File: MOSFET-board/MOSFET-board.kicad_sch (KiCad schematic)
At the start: 5 parts, among them J1 PCIE-LP-01-01-F-DV-A-TR, J2 DB15_Female, J3 DB15_Female, U11 PCF8575_Breakout

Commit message: Progress on revising ground boards.
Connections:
- net +12V: no longer J2.10 (P10), J2.11 (P111), J2.12 (P12), J2.13 (P13), J2.9 (P9), J3.10 (P10), J3.11 (P111), J3.12 (P12), J3.13 (P13), J3.9 (P9)
- new net -7 V: J2.10 (P10), J2.11 (P111), J2.12 (P12), J2.13 (P13), J2.9 (P9), J3.10 (P10), J3.11 (P111), J3.12 (P12), J3.13 (P13), J3.9 (P9)

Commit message: Further revision. Two batteries system.
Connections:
- net -7 V renamed -7V
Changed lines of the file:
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@@
+    (stroke (width 0) (type default))
+  )
+  (wire (pts (xy 175.006 113.03) (xy 175.006 114.808))
     (stroke (width 0) (type default))
   )
@@
     )
   )
+  (global_label "BAT2_+" (shape input) (at 169.418 114.808 270) (fields_autoplaced)
+    (effects (font (size 1.27 1.27)) (justify right))
+    (property "Intersheetrefs" "${INTERSHEET_REFS}" (at 169.418 124.8689 90)
+      (effects (font (size 1.27 1.27)) (justify right) hide)
+    )
+  )
   (global_label "I2C_SDA" (shape input) (at 46.99 120.65 270) (fields_autoplaced)
     (effects (font (size 1.27 1.27)) (justify right))
@@
     )
   )
+  (global_label "-7V" (shape input) (at 175.006 113.03 0) (fields_autoplaced)
+    (effects (font (size 1.27 1.27)) (justify left))
+    (property "Intersheetrefs" "${INTERSHEET_REFS}" (at 181.8617 113.03 0)
+      (effects (font (size 1.27 1.27)) (justify left) hide)
+    )
+  )
   (global_label "PYRO9" (shape input) (at 165.608 78.232 180) (fields_autoplaced)
     (effects (font (size 1.27 1.27)) (justify right))
@@
     )
   )
-  (global_label "-7 V" (shape input) (at 26.416 167.132 270) (fields_autoplaced)
-    (effects (font (size 1.27 1.27)) (justify right))
-    (property "Intersheetrefs" "${INTERSHEET_REFS}" (at 26.416 174.9553 90)
+  (global_label "BAT2_-" (shape input) (at 26.416 167.132 270) (fields_autoplaced)
+    (effects (font (size 1.27 1.27)) (justify right))
+    (property "Intersheetrefs" "${INTERSHEET_REFS}" (at 26.416 177.1929 90)
       (effects (font (size 1.27 1.27)) (justify right) hide)
     )
@@
     )
   )
-  (global_label "-7 V" (shape input) (at 68.326 166.878 270) (fields_autoplaced)
-    (effects (font (size 1.27 1.27)) (justify right))
-    (property "Intersheetrefs" "${INTERSHEET_REFS}" (at 68.326 174.7013 90)
+  (global_label "BAT2_-" (shape input) (at 68.326 166.878 270) (fields_autoplaced)
+    (effects (font (size 1.27 1.27)) (justify right))
+    (property "Intersheetrefs" "${INTERSHEET_REFS}" (at 68.326 176.9389 90)
+      (effects (font (size 1.27 1.27)) (justify right) hide)
+    )
+  )
+  (global_label "BAT2_-" (shape input) (at 175.006 114.808 270) (fields_autoplaced)
+    (effects (font (size 1.27 1.27)) (justify right))
+    (property "Intersheetrefs" "${INTERSHEET_REFS}" (at 175.006 124.8689 90)
       (effects (font (size 1.27 1.27)) (justify right) hide)
     )
@@
         )
       )
+    )
+  )
+  (symbol (lib_id "power:+5V") (at 169.418 114.808 0) (unit 1)
+    (in_bom yes) (on_board yes) (dnp no)
+    (property "Reference" "#PWR010" (at 169.418 118.618 0)
+      (effects (font (size 1.27 1.27)) hide)
+    )
+    (property "Value" "+5V" (at 168.91 110.49 0)
+      (effects (font (size 1.27 1.27)))
+    )
+    (property "Footprint" "" (at 169.418 114.808 0)
+      (effects (font (size 1.27 1.27)) hide)
+    )
+    (property "Datasheet" "" (at 169.418 114.808 0)
+      (effects (font (size 1.27 1.27)) hide)
+    )
+    (pin "1")
+    (instances
+      (project "MOSFET-board"
+        (path "/eeff6235-4c56-4b47-a90f-883101560994"
+          (reference "#PWR010") (unit 1)
+        )
+      )

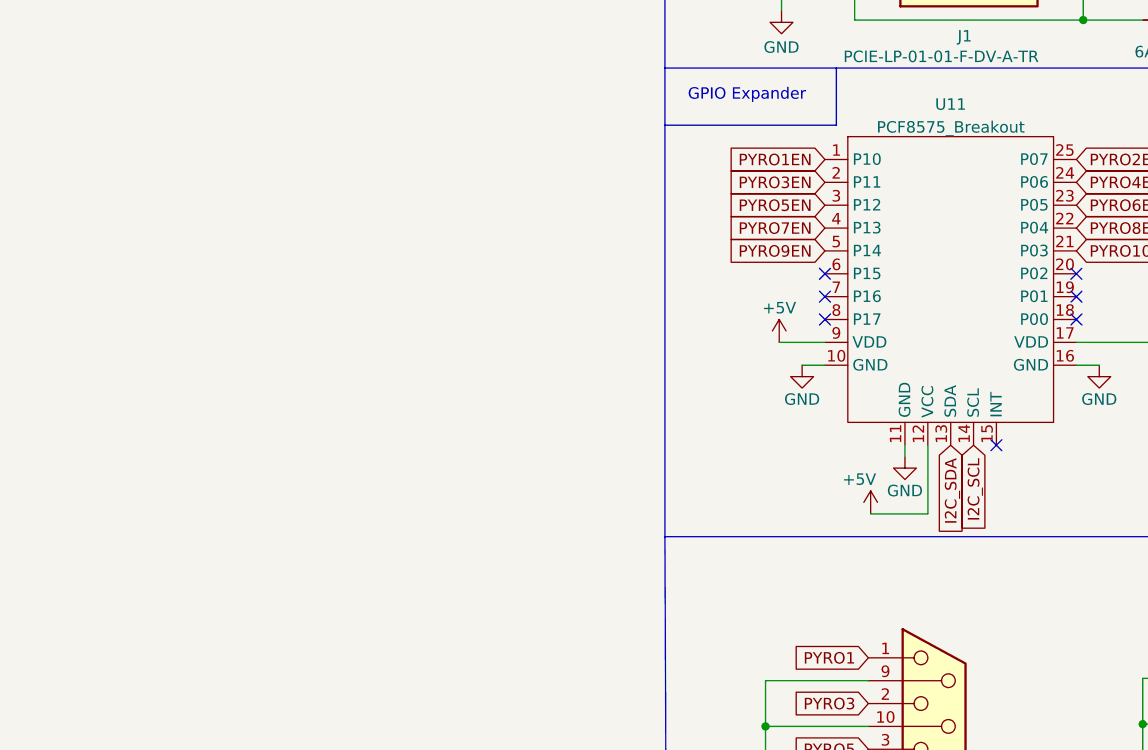
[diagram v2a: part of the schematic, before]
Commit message: Added level shifter for gpio expander.
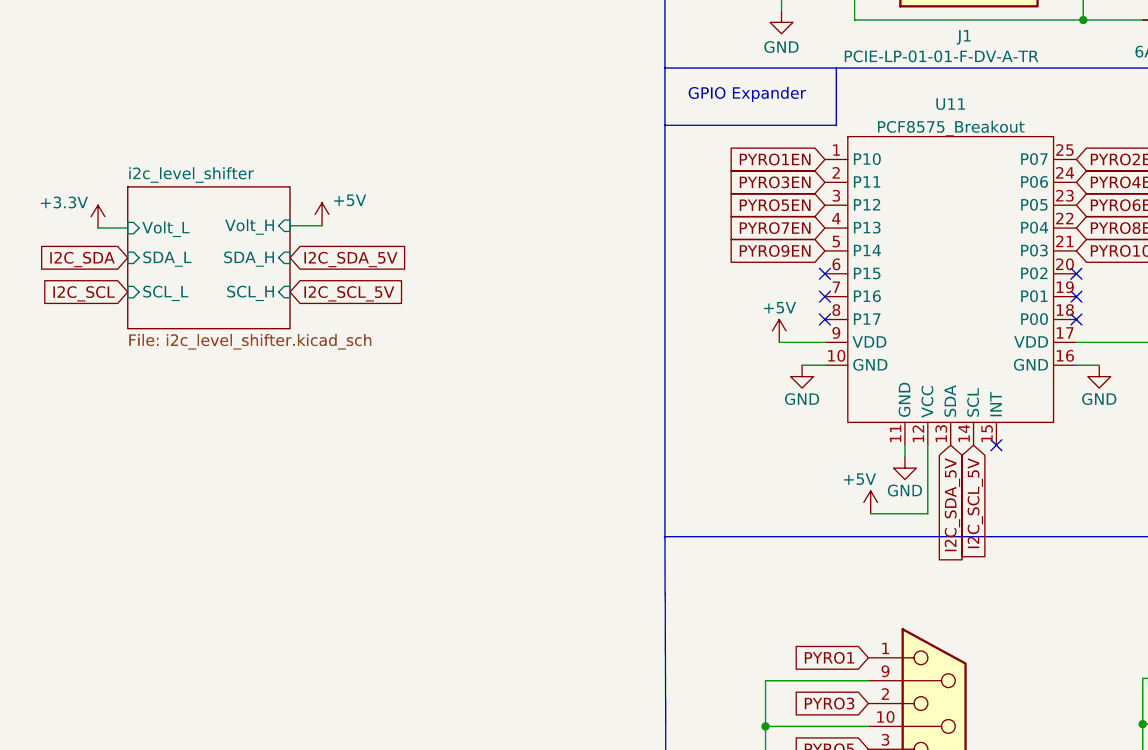
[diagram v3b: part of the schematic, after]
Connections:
- net I2C_SCL: no longer U11.14 (SCL)
- net I2C_SDA: no longer U11.13 (SDA)
- new net I2C_SCL_5V: U11.14 (SCL)
- new net I2C_SDA_5V: U11.13 (SDA)
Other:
- added sheet i2c_level_shifter (i2c_level_shifter.kicad_sch)
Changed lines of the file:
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@@
+    (stroke (width 0) (type default))
+  )
+  (wire (pts (xy -26.416 96.266) (xy -22.86 96.266))
     (stroke (width 0) (type default))
   )
@@
   )
   (wire (pts (xy 68.326 151.638) (xy 68.326 156.718))
+    (stroke (width 0) (type default))
+  )
+  (wire (pts (xy -47.752 96.52) (xy -44.45 96.52))
     (stroke (width 0) (type default))
   )
@@
     )
   )
-  (global_label "I2C_SDA" (shape input) (at 46.99 120.65 270) (fields_autoplaced)
-    (effects (font (size 1.27 1.27)) (justify right))
-    (property "Intersheetrefs" "${INTERSHEET_REFS}" (at 46.9106 130.6831 90)
+  (global_label "I2C_SDA" (shape input) (at -44.45 99.822 180) (fields_autoplaced)
+    (effects (font (size 1.27 1.27)) (justify right))
+    (property "Intersheetrefs" "${INTERSHEET_REFS}" (at -55.0552 99.822 0)
       (effects (font (size 1.27 1.27)) (justify right) hide)
     )
@@
     )
   )
-  (global_label "I2C_SCL" (shape input) (at 49.53 120.65 270) (fields_autoplaced)
-    (effects (font (size 1.27 1.27)) (justify right))
-    (property "Intersheetrefs" "${INTERSHEET_REFS}" (at 49.4506 130.6226 90)
+  (global_label "I2C_SCL" (shape input) (at -44.45 103.632 180) (fields_autoplaced)
+    (effects (font (size 1.27 1.27)) (justify right))
+    (property "Intersheetrefs" "${INTERSHEET_REFS}" (at -54.9947 103.632 0)
       (effects (font (size 1.27 1.27)) (justify right) hide)
     )
@@
     (property "Intersheetrefs" "${INTERSHEET_REFS}" (at 90.0913 104.3146 0)
       (effects (font (size 1.27 1.27)) (justify right) hide)
+    )
+  )
+  (global_label "I2C_SDA_5V" (shape input) (at -26.416 99.822 0) (fields_autoplaced)
+    (effects (font (size 1.27 1.27)) (justify left))
+    (property "Intersheetrefs" "${INTERSHEET_REFS}" (at -12.5451 99.822 0)
+      (effects (font (size 1.27 1.27)) (justify left) hide)
     )
   )
@@
     )
   )
+  (global_label "I2C_SCL_5V" (shape input) (at -26.416 103.632 0) (fields_autoplaced)
+    (effects (font (size 1.27 1.27)) (justify left))
+    (property "Intersheetrefs" "${INTERSHEET_REFS}" (at -12.6056 103.632 0)
+      (effects (font (size 1.27 1.27)) (justify left) hide)
+    )
+  )
   (global_label "PYRO9EN" (shape input) (at 33.02 99.06 180) (fields_autoplaced)
     (effects (font (size 1.27 1.27)) (justify right))
@@
     (effects (font (size 1.27 1.27)) (justify right))
     (property "Intersheetrefs" "${INTERSHEET_REFS}" (at 90.7928 81.9626 0)
+      (effects (font (size 1.27 1.27)) (justify right) hide)
+    )
+  )
+  (global_label "I2C_SCL_5V" (shape input) (at 49.53 120.65 270) (fields_autoplaced)
+    (effects (font (size 1.27 1.27)) (justify right))
+    (property "Intersheetrefs" "${INTERSHEET_REFS}" (at 49.53 134.4604 90)
       (effects (font (size 1.27 1.27)) (justify right) hide)
     )
@@
     (effects (font (size 1.27 1.27)) (justify right))
     (property "Intersheetrefs" "${INTERSHEET_REFS}" (at 21.4661 96.52 0)
+      (effects (font (size 1.27 1.27)) (justify right) hide)
+    )
+  )
+  (global_label "I2C_SDA_5V" (shape input) (at 46.99 120.65 270) (fields_autoplaced)
+    (effects (font (size 1.27 1.27)) (justify right))
+    (property "Intersheetrefs" "${INTERSHEET_REFS}" (at 46.99 134.5209 90)
       (effects (font (size 1.27 1.27)) (justify right) hide)
     )
@@
     )
   )
+  (symbol (lib_id "power:+3.3V") (at -47.752 96.52 0) (unit 1)
+    (in_bom yes) (on_board yes) (dnp no)
+    (property "Reference" "#PWR015" (at -47.752 100.33 0)
+      (effects (font (size 1.27 1.27)) hide)
+    )
+    (property "Value" "+3.3V" (at -51.562 93.726 0)
+      (effects (font (size 1.27 1.27)))
+    )
+    (property "Footprint" "" (at -47.752 96.52 0)
+      (effects (font (size 1.27 1.27)) hide)
+    )
+    (property "Datasheet" "" (at -47.752 96.52 0)
+      (effects (font (size 1.27 1.27)) hide)
+    )
+    (pin "1")
+    (instances
+      (project "MOSFET-board"
+        (path "/eeff6235-4c56-4b47-a90f-883101560994"
+          (reference "#PWR015") (unit 1)
+        )
+      )
+    )
+  )
   (symbol (lib_id "power:+3.3V") (at 163.83 139.446 0) (unit 1)
     (in_bom yes) (on_board yes) (dnp no)
@@
         (path "/eeff6235-4c56-4b47-a90f-883101560994"
           (reference "#PWR02") (unit 1)
+        )
+      )
+    )
+  )
+  (symbol (lib_id "power:+5V") (at -22.86 96.266 0) (unit 1)
+    (in_bom yes) (on_board yes) (dnp no)
+    (property "Reference" "#PWR016" (at -22.86 100.076 0)
+      (effects (font (size 1.27 1.27)) hide)
+    )
+    (property "Value" "+5V" (at -19.812 93.472 0)
+      (effects (font (size 1.27 1.27)))
+    )
+    (property "Footprint" "" (at -22.86 96.266 0)
+      (effects (font (size 1.27 1.27)) hide)
+    )
+    (property "Datasheet" "" (at -22.86 96.266 0)
+      (effects (font (size 1.27 1.27)) hide)
+    )
+    (pin "1")
+    (instances
+      (project "MOSFET-board"
+        (path "/eeff6235-4c56-4b47-a90f-883101560994"
+          (reference "#PWR016") (unit 1)
         )
       )
@@
       )
     )
+  )
+  (sheet (at -44.45 91.948) (size 18.034 15.748) (fields_autoplaced)
+    (stroke (width 0.1524) (type solid))
+    (fill (color 0 0 0 0.0000))
+    (property "Sheetname" "i2c_level_shifter" (at -44.45 91.2364 0)
+      (effects (font (size 1.27 1.27)) (justify left bottom))
+    )
+    (property "Sheetfile" "i2c_level_shifter.kicad_sch" (at -44.45 108.2806 0)
+      (effects (font (size 1.27 1.27)) (justify left top))
+    )
+    (pin "Volt_H" input (at -26.416 96.266 0)
+      (effects (font (size 1.27 1.27)) (justify right))
+    )
+    (pin "SDA_H" input (at -26.416 99.822 0)
+      (effects (font (size 1.27 1.27)) (justify right))
+    )
+    (pin "Volt_L" input (at -44.45 96.52 180)
+      (effects (font (size 1.27 1.27)) (justify left))
+    )
+    (pin "SCL_H" input (at -26.416 103.632 0)
+      (effects (font (size 1.27 1.27)) (justify right))
+    )
+    (pin "SCL_L" input (at -44.45 103.632 180)
+      (effects (font (size 1.27 1.27)) (justify left))
+    )
+    (pin "SDA_L" input (at -44.45 99.822 180)
+      (effects (font (size 1.27 1.27)) (justify left))
+    )
+    (instances
+      (project "MOSFET-board"
+        (path "/eeff6235-4c56-4b47-a90f-883101560994" (page "12"))
+      )
+    )

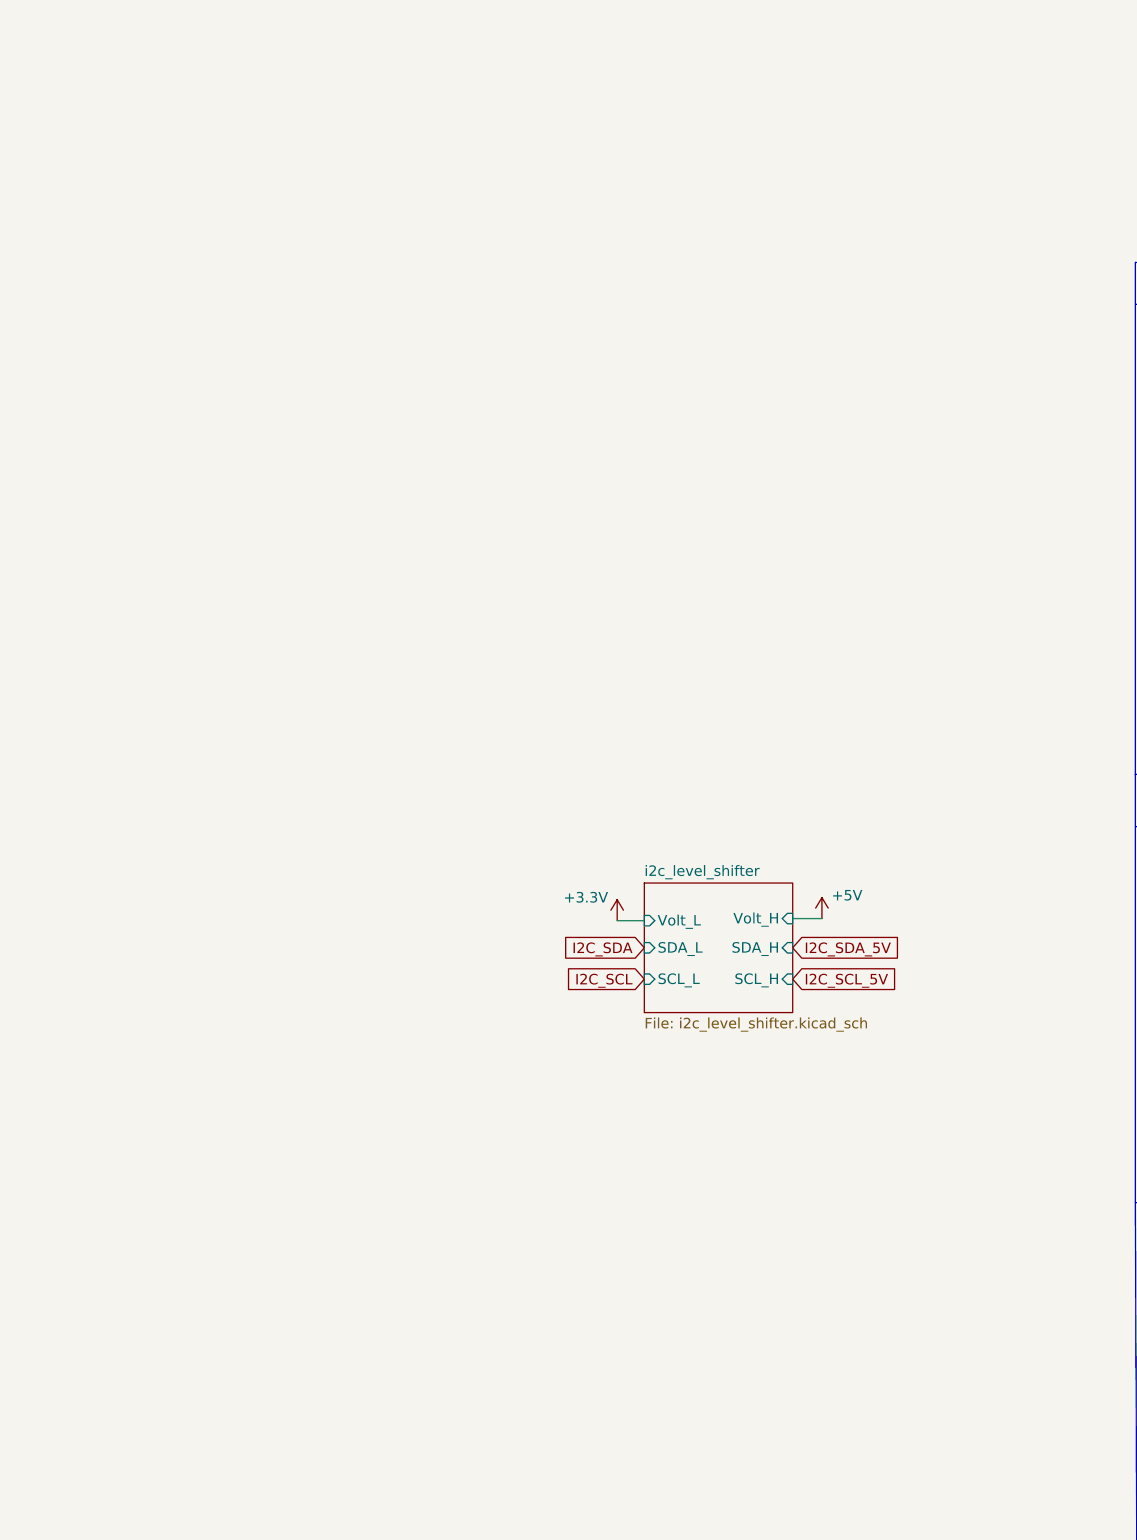
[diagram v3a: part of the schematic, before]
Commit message: Revising PCIe.
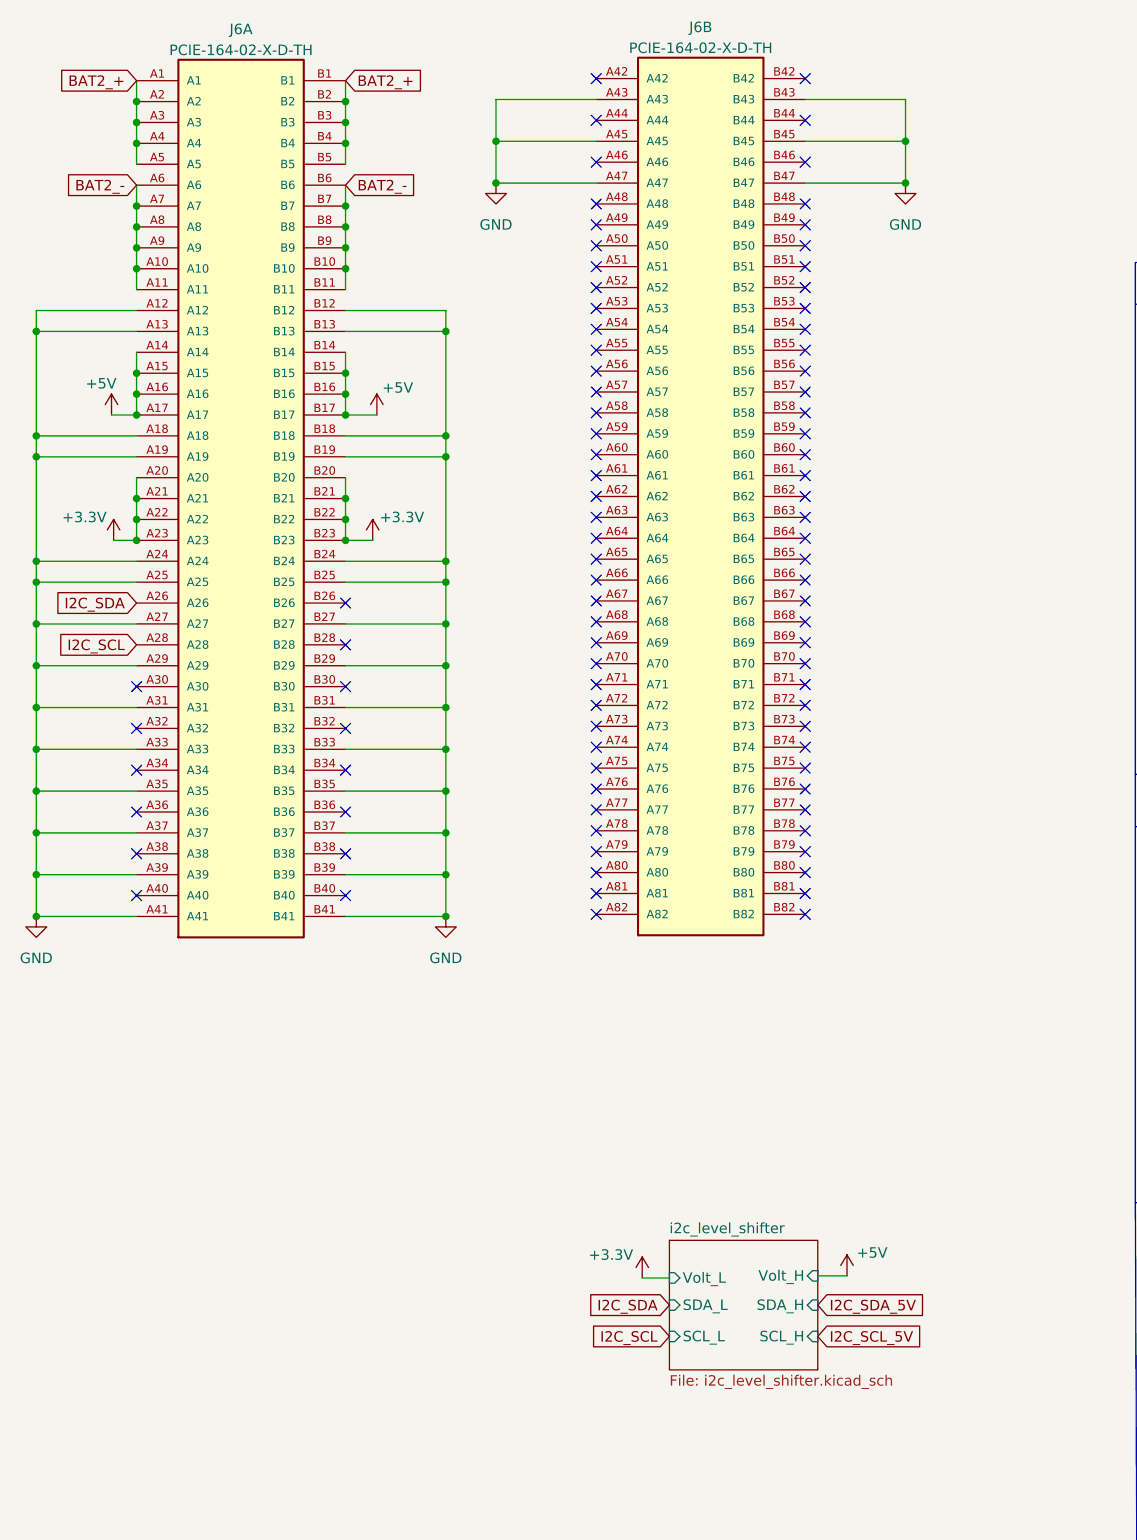
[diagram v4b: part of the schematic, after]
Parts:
- added J6: PCIE-164-02-X-D-TH, PCIE-164-02-X-D-TH:SAMTEC_PCIE-164-02-X-D-TH, symbol PCIE-164-02-X-D-TH:PCIE-164-02-X-D-TH
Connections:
- net +3.3V: now also J6.A20, J6.A21, J6.A22, J6.A23, J6.B20, J6.B21, J6.B22, J6.B23
- net +5V: now also J6.A1, J6.A14, J6.A15, J6.A16, J6.A17, J6.A2, J6.A3, J6.A4, J6.A5, J6.B1, J6.B14, J6.B15, J6.B16, J6.B17, J6.B2, J6.B3, J6.B4, J6.B5
- net -7V: now also J6.A10, J6.A11, J6.A6, J6.A7, J6.A8, J6.A9, J6.B10, J6.B11, J6.B6, J6.B7, J6.B8, J6.B9
- net GND: now also J6.A12, J6.A13, J6.A18, J6.A19, J6.A24, J6.A25, J6.A27, J6.A29, J6.A31, J6.A33, J6.A35, J6.A37, J6.A39, J6.A41, J6.A43, J6.A45, J6.A47, J6.B12, J6.B13, J6.B18, J6.B19, J6.B24, J6.B25, J6.B27, J6.B29, J6.B31, J6.B33, J6.B35, J6.B37, J6.B39, J6.B41, J6.B43, J6.B45, J6.B47
- net I2C_SCL: now also J6.A28
- net I2C_SDA: now also J6.A26
- no-connect marks 34 -> 124
